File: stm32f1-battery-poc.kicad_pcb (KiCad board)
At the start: 4 copper layers, 92.5 x 85 mm, 153 parts, among them J1 Conn_01x02, J10 Conn_02x03_Odd_Even, J11 Conn_02x03_Odd_Even, J12 Conn_02x03_Odd_Even, J2 Conn_02x02_Odd_Even, J3 Conn_02x03_Odd_Even, J4 Conn_02x07_Odd_Even, J5 Conn_02x02_Odd_Even, J6 Conn_02x02_Odd_Even, J7 Conn_02x03_Odd_Even, J8 Conn_01x02, J9 Conn_01x04_Pin, M1 Stepper_Motor_bipolar, M2 Motor_3_Phases, Q1 Q_NMOS, Q2 Q_NMOS, SW1 SW_Push, SW2 SW_Push, SW3 SW_Push, SW4 SW_SPST, U1 LM78M05, U10 DRV8311H, U2 HT753-1, U3 SN65HVD230, U4 QRE1113GR, U5 QRE1113GR, U6 QRE1113GR, U7 DRV8424RGER, U8 STM32F103C8Tx, U9 BQ77905, Y1 8M

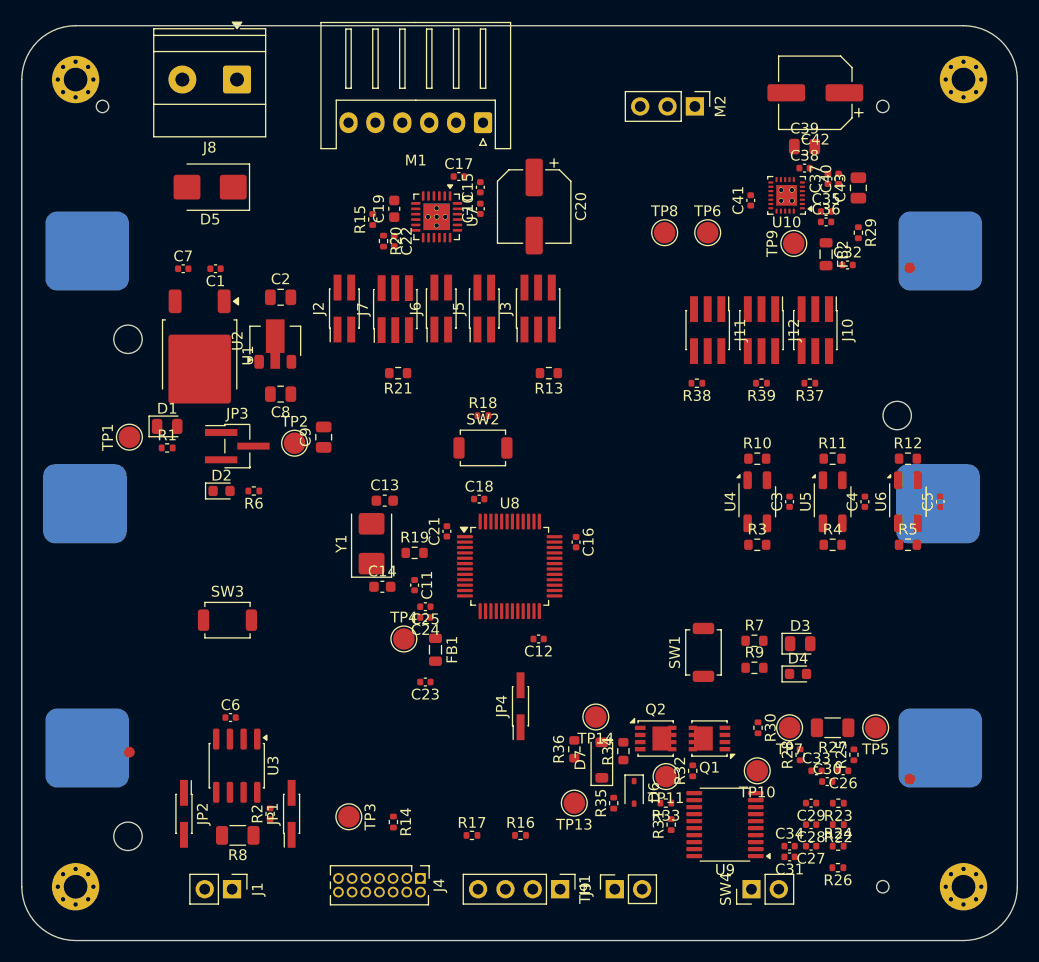
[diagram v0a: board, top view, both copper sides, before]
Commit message: pcb: add gnd planes
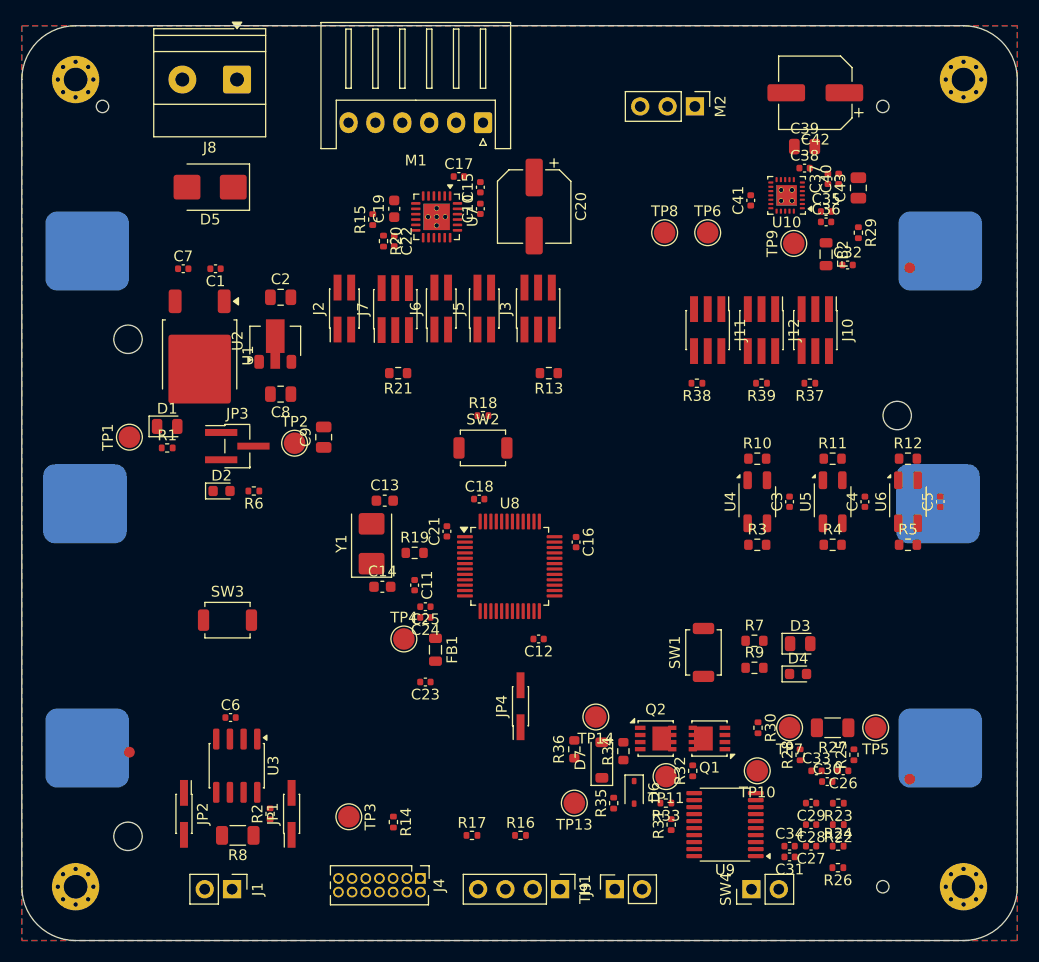
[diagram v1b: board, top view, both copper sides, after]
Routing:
- added copper zone on B.Cu, net GND
- added copper zone on F.Cu, net GND
- added copper zone on In1.Cu, net GND
- added copper zone on In2.Cu, net GND
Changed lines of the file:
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@@
 		(net 3)
+	)
+	(zone
+		(net 5)
+		(net_name "GND")
+		(layers "F.Cu" "B.Cu" "In1.Cu" "In2.Cu")
+		(hatch edge 0.5)
+		(connect_pads
+			(clearance 0.2)
+		)
+		(min_thickness 0.15)
+		(filled_areas_thickness no)
+		(fill yes
+			(thermal_gap 0.35)
+			(thermal_bridge_width 0.35)
+		)
+		(polygon
+			(pts
+				(xy 195 42.5) (xy 102.5 42.5) (xy 102.5 127.5) (xy 195 127.5)
+			)
+		)
 	)
 	(embedded_fonts no)

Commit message: pcb: add gnd vias
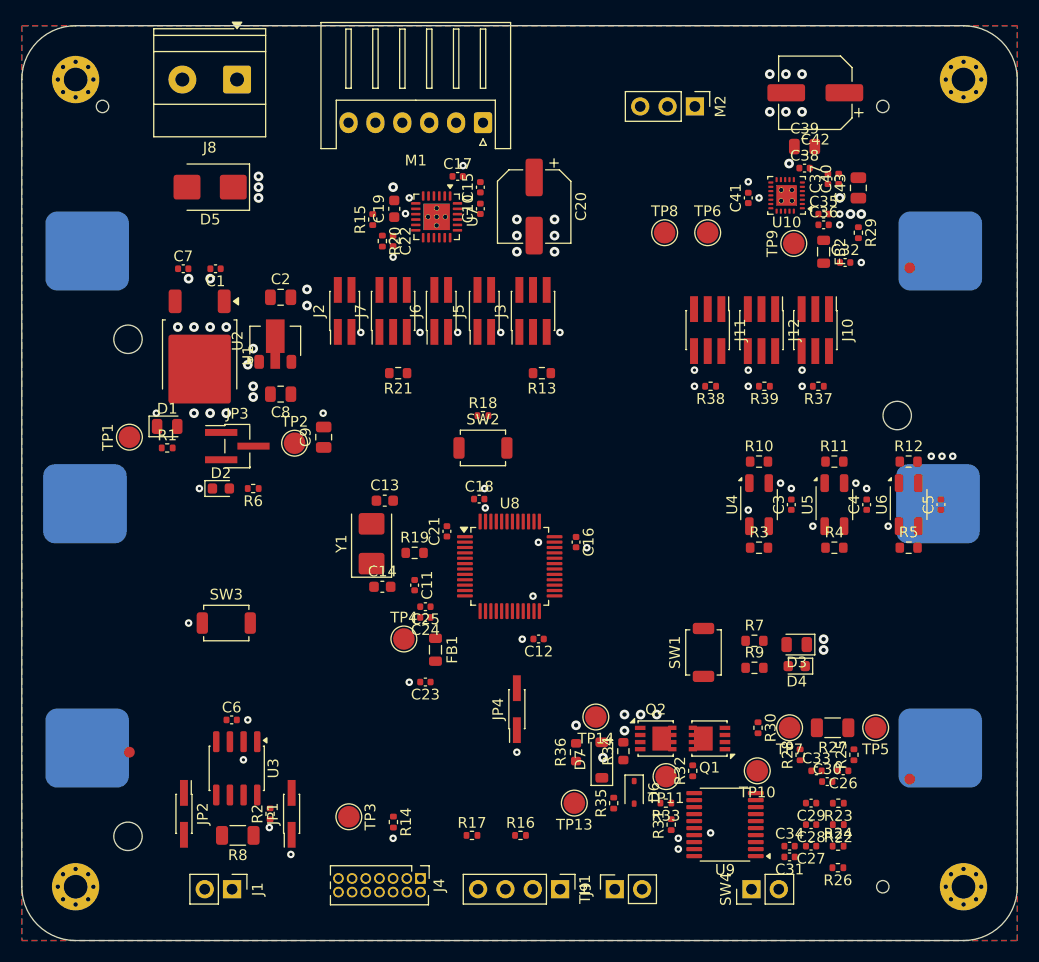
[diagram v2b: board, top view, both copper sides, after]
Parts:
- moved R38 1.30 mm to (166.5, 76.0)
- moved R37 0.84 mm to (176.5, 76.0)
- moved D4 0.74 mm to (174.5, 102.0), turned to 180 degrees
- moved R13 0.65 mm to (150.8, 74.8)
- moved J3 0.52 mm to (150.0, 69.0)
- moved JP4 0.43 mm to (148.5, 106.0)
- moved R39 0.39 mm to (171.5, 76.0)
- moved C36 0.35 mm to (177.0, 61.0)
- moved D3 0.34 mm to (174.5, 100.0), turned to 180 degrees
- moved C35 0.33 mm to (177.0, 60.0)
- moved C32 0.33 mm to (179.0, 64.5)
- moved C41 0.33 mm to (170.0, 58.5)
- moved FB2 0.33 mm to (177.0, 63.5)
- moved C3 0.32 mm to (174.0, 87.0)
- moved C4 0.32 mm to (181.0, 87.0)
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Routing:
- net GND: vias 0 -> 93

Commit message: schem: change I2C pins
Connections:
- J9 pad 2: /I2C1_SDA -> /I2C2_SDA
- J9 pad 4: /I2C1_SCL -> /I2C2_SCL
- R16 pad 1: /I2C1_SDA -> /I2C2_SDA
- R17 pad 1: /I2C1_SCL -> /I2C2_SCL
- U8 pad 21: unconnected-(U8-PB10-Pad21) -> /I2C2_SCL
- U8 pad 22: unconnected-(U8-PB11-Pad22) -> /I2C2_SDA
- U8 pad 45: /I2C1_SCL -> unconnected-(U8-PB8-Pad45)
- U8 pad 46: /I2C1_SDA -> unconnected-(U8-PB9-Pad46)

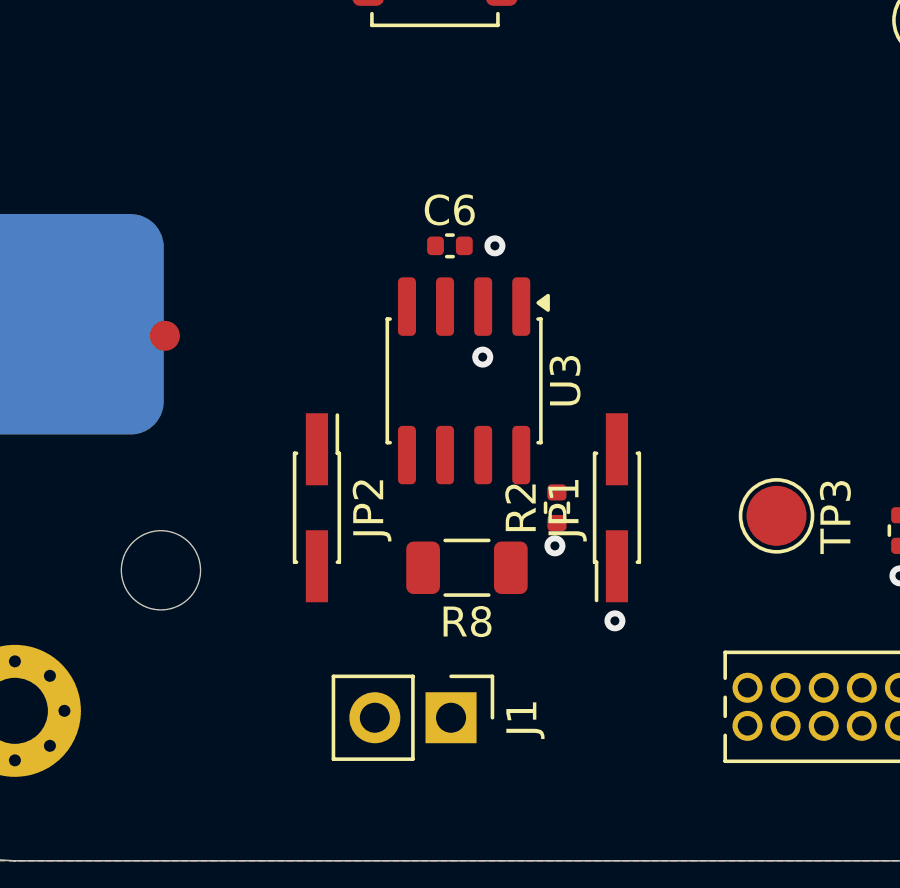
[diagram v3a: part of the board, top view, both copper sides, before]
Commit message: pcb: add CAN layout
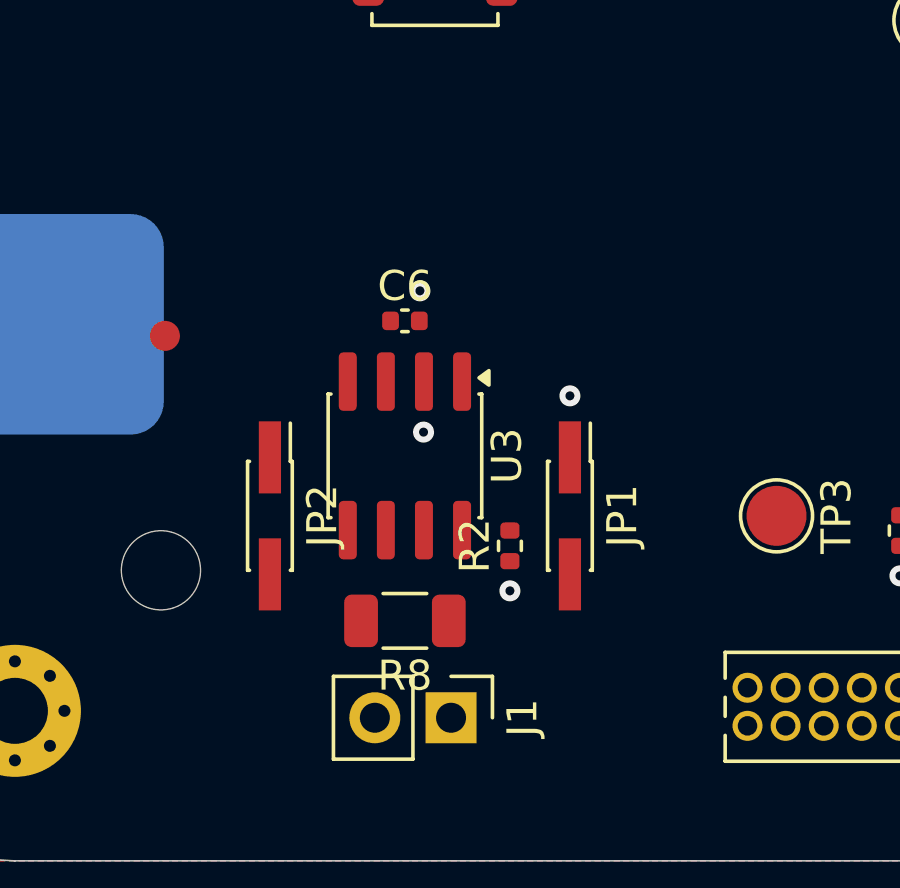
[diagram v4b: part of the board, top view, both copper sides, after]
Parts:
- moved U3 3.18 mm to (120.5, 114.0)
- moved C6 2.92 mm to (120.5, 109.5)
- moved R8 2.72 mm to (120.5, 119.5)
- moved R2 2.02 mm to (124.0, 117.0)
- moved JP1 1.59 mm to (126.0, 116.0), turned to -90 degrees
- moved JP2 1.59 mm to (116.0, 116.0)
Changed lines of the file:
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@@
 	(footprint "Connector_PinHeader_1.27mm:PinHeader_2x01_P1.27mm_Vertical_SMD"
 		(layer "F.Cu")
-		(at 117.5675 115.73 -90)
+		(at 116 116 -90)
 		(descr "surface-mounted straight pin header, 2x01, 1.27mm pitch, double rows")
 		(tags "Surface mounted pin header SMD 2x01 1.27mm double row")
@@
 	(footprint "Capacitor_SMD:C_0402_1005Metric"
 		(layer "F.Cu")
-		(at 122 107)
+		(at 120.5 109.5)
 		(descr "Capacitor SMD 0402 (1005 Metric), square (rectangular) end terminal, IPC-7351 nominal, (Body size source: IPC-SM-782 page 76, https://www.pcb-3d.com/wordpress/wp-content/uploads/ipc-sm-782a_amendment_1_and_2.pdf), generated with kicad-footprint-generator")
 		(tags "capacitor")
@@
 	(footprint "Resistor_SMD:R_0402_1005Metric"
 		(layer "F.Cu")
-		(at 125.5675 115.73 90)
+		(at 124 117 90)
 		(descr "Resistor SMD 0402 (1005 Metric), square (rectangular) end terminal, IPC-7351 nominal, (Body size source: IPC-SM-782 page 72, https://www.pcb-3d.com/wordpress/wp-content/uploads/ipc-sm-782a_amendment_1_and_2.pdf), generated with kicad-footprint-generator")
 		(tags "resistor")
@@
 	(footprint "Connector_PinHeader_1.27mm:PinHeader_2x01_P1.27mm_Vertical_SMD"
 		(layer "F.Cu")
-		(at 127.5675 115.73 90)
+		(at 126 116 -90)
 		(descr "surface-mounted straight pin header, 2x01, 1.27mm pitch, double rows")
 		(tags "Surface mounted pin header SMD 2x01 1.27mm double row")
@@
 		(attr smd exclude_from_bom)
 		(fp_line
-			(start 1.815 -0.745)
-			(end 1.815 -0.68)
+			(start -1.815 0.745)
+			(end 1.815 0.745)
 			(stroke
 				(width 0.12)
@@
 		)
 		(fp_line
-			(start -1.815 -0.745)
-			(end 1.815 -0.745)
+			(start -1.815 0.68)
+			(end -1.815 0.745)
 			(stroke
 				(width 0.12)
@@
 		)
 		(fp_line
-			(start -1.815 -0.745)
-			(end -1.815 -0.68)
+			(start 1.815 0.68)
+			(end 1.815 0.745)
 			(stroke
 				(width 0.12)
@@
 		)
 		(fp_line
-			(start 1.815 0.68)
-			(end 1.815 0.745)
+			(start -1.815 -0.745)
+			(end -1.815 -0.68)
 			(stroke
 				(width 0.12)
@@
 		)
 		(fp_line
-			(start -1.815 0.68)
-			(end -1.815 0.745)
+			(start -1.815 -0.745)
+			(end 1.815 -0.745)
 			(stroke
 				(width 0.12)
@@
 		)
 		(fp_line
-			(start -1.815 0.745)
-			(end 1.815 0.745)
+			(start 1.815 -0.745)
+			(end 1.815 -0.68)
 			(stroke
 				(width 0.12)
@@
 		)
 		(fp_line
-			(start 4.29 -1.14)
-			(end -4.29 -1.14)
+			(start -4.29 1.14)
+			(end 4.29 1.14)
 			(stroke
 				(width 0.05)
@@
 		)
 		(fp_line
-			(start -4.29 -1.14)
-			(end -4.29 1.14)
+			(start 4.29 1.14)
+			(end 4.29 -1.14)
 			(stroke
 				(width 0.05)
@@
 		)
 		(fp_line
-			(start 4.29 1.14)
-			(end 4.29 -1.14)
+			(start -4.29 -1.14)
+			(end -4.29 1.14)
 			(stroke
 				(width 0.05)
@@
 		)
 		(fp_line
-			(start -4.29 1.14)
-			(end 4.29 1.14)
+			(start 4.29 -1.14)
+			(end -4.29 -1.14)
 			(stroke
 				(width 0.05)
@@
 		)
 		(fp_line
-			(start 1.705 -0.635)
-			(end 1.705 0.635)
+			(start -1.705 0.635)
+			(end -1.705 -0.2)
 			(stroke
 				(width 0.1)
@@
 		)
 		(fp_line
-			(start -1.27 -0.635)
-			(end 1.705 -0.635)
+			(start 1.705 0.635)
+			(end -1.705 0.635)
 			(stroke
 				(width 0.1)
@@
 		)
 		(fp_line
-			(start 2.75 -0.2)
-			(end 2.75 0.2)
+			(start -2.75 0.2)
+			(end -1.705 0.2)
 			(stroke
 				(width 0.1)
@@
 		)
 		(fp_line
-			(start 1.705 -0.2)
-			(end 2.75 -0.2)
+			(start 2.75 0.2)
+			(end 1.705 0.2)
 			(stroke
 				(width 0.1)
@@
 		)
 		(fp_line
-			(start -1.705 -0.2)
-			(end -1.27 -0.635)
+			(start -2.75 -0.2)
+			(end -2.75 0.2)
 			(stroke
 				(width 0.1)
@@
 		)
 		(fp_line
-			(start -2.75 -0.2)
-			(end -2.75 0.2)
+			(start -1.705 -0.2)
+			(end -1.27 -0.635)
 			(stroke
 				(width 0.1)
@@
 		)
 		(fp_line
-			(start 2.75 0.2)
-			(end 1.705 0.2)
+			(start 1.705 -0.2)
+			(end 2.75 -0.2)
 			(stroke
 				(width 0.1)
@@
 		)
 		(fp_line
-			(start -2.75 0.2)
-			(end -1.705 0.2)
+			(start 2.75 -0.2)
+			(end 2.75 0.2)
 			(stroke
 				(width 0.1)
@@
 		)
 		(fp_line
-			(start 1.705 0.635)
-			(end -1.705 0.635)
+			(start -1.27 -0.635)
+			(end 1.705 -0.635)
 			(stroke
 				(width 0.1)
@@
 		)
 		(fp_line
-			(start -1.705 0.635)
-			(end -1.705 -0.2)
+			(start 1.705 -0.635)
+			(end 1.705 0.635)
 			(stroke
 				(width 0.1)
@@
 		)
 		(pad "1" smd rect
-			(at -1.95 0 90)
+			(at -1.95 0 270)
 			(size 2.4 0.74)
 			(layers "F.Cu" "F.Mask" "F.Paste")
@@
 		)
 		(pad "2" smd rect
-			(at 1.95 0 90)
+			(at 1.95 0 270)
 			(size 2.4 0.74)
 			(layers "F.Cu" "F.Mask" "F.Paste")
@@
 	(footprint "Package_SO:SOIC-8_3.9x4.9mm_P1.27mm"
 		(layer "F.Cu")
-		(at 122.4725 111.5 -90)
+		(at 120.5 114 -90)
 		(descr "SOIC, 8 Pin (JEDEC MS-012AA, https://www.analog.com/media/en/package-pcb-resources/package/pkg_pdf/soic_narrow-r/r_8.pdf), generated with kicad-footprint-generator ipc_gullwing_generator.py")
 		(tags "SOIC SO")
@@
 	(footprint "Resistor_SMD:R_1206_3216Metric"
 		(layer "F.Cu")
-		(at 122.5675 117.73 180)
+		(at 120.5 119.5 180)
 		(descr "Resistor SMD 1206 (3216 Metric), square (rectangular) end terminal, IPC-7351 nominal, (Body size source: IPC-SM-782 page 72, https://www.pcb-3d.com/wordpress/wp-content/uploads/ipc-sm-782a_amendment_1_and_2.pdf), generated with kicad-footprint-generator")
 		(tags "resistor")
@@
 	)
 	(via
-		(at 125.5 117)
+		(at 124 118.5)
 		(size 0.7)
 		(drill 0.3)
@@
 	)
 	(via
-		(at 123.093312 110.708542)
+		(at 121.120812 113.208542)
 		(size 0.7)
 		(drill 0.3)
@@
 	)
 	(via
-		(at 123.5 107)
+		(at 121 108.5)
 		(size 0.7)
 		(drill 0.3)
@@
 	)
 	(via
-		(at 127.5 119.5)
+		(at 126 112)
 		(size 0.7)
 		(drill 0.3)

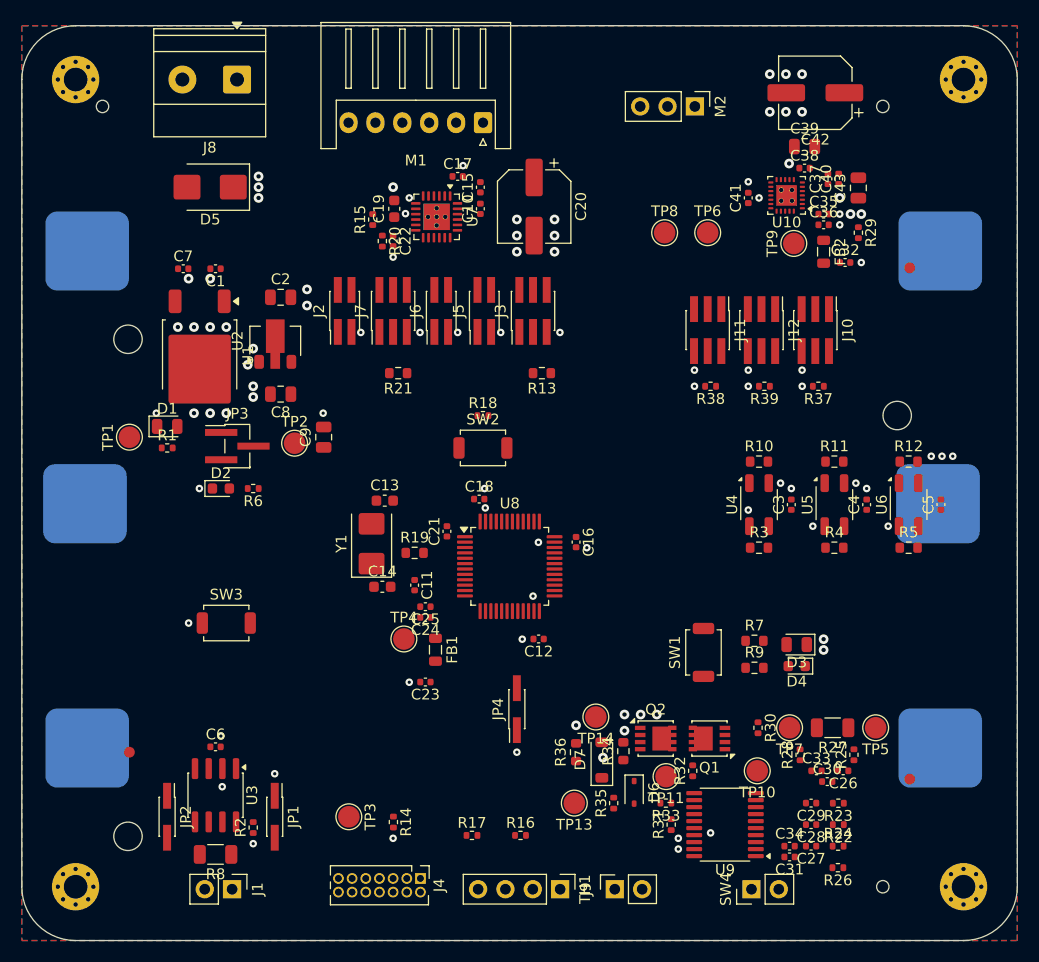
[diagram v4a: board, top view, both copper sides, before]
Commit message: pcb: add STDC14 debug port routing
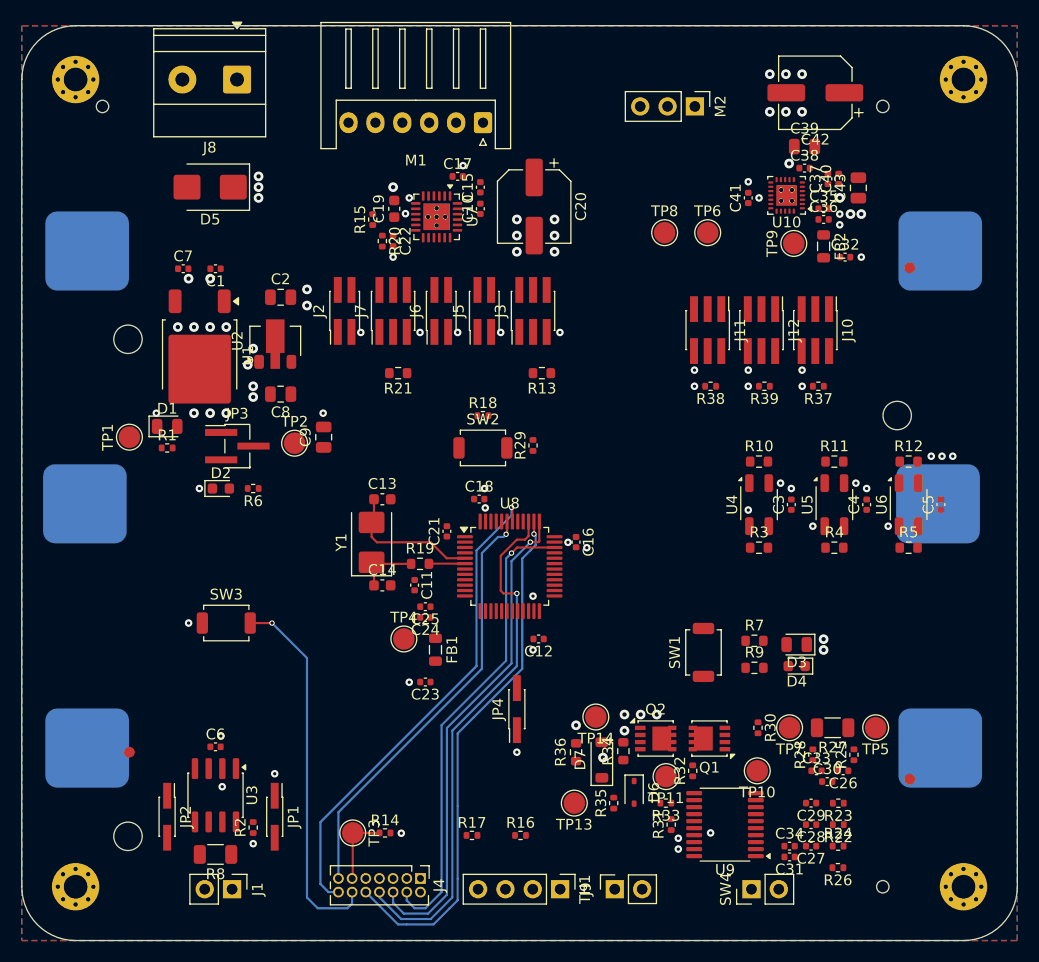
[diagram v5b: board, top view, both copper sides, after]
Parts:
- moved R29 36.1 mm to (150.0, 81.5), turned to 90 degrees
- moved TP3 1.54 mm to (133.2, 117.5)
- moved R14 1.27 mm to (136.2, 117.5), turned to 0 degrees
- moved R28 1.18 mm to (176.0, 110.2)
- moved R19 1.14 mm to (139.5, 92.5)
- moved C32 0.50 mm to (179.0, 64.0)
- moved C35 0.50 mm to (177.0, 59.5)
- moved C36 0.50 mm to (177.0, 60.5)
- moved FB2 0.50 mm to (177.0, 63.0)
- moved C13 0.26 mm to (136.0, 86.5)
- moved C14 0.13 mm to (136.0, 94.5)
- moved Y1 0.13 mm to (135.0, 90.5)
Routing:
- net /SYS_JTDO: track 0.00 -> 49.2 mm, vias 0 -> 1
- net /SYS_JTDI: track 0.00 -> 49.0 mm, vias 0 -> 1
- net /SYS_JTCK: track 0.00 -> 45.8 mm, vias 0 -> 1
- net /USART1_TX: track 0.00 -> 45.7 mm, vias 0 -> 1
- net /SYS_JTMS: track 0.00 -> 43.3 mm, vias 0 -> 1
- net /USART1_RX: track 0.00 -> 39.9 mm, vias 0 -> 1
- net /NRST: track 0.00 -> 34.7 mm, vias 0 -> 1
- net /XTAL_I: track 0.00 -> 13.1 mm
- net Net-(J4-Pin_11): track 0.00 -> 6.74 mm
- net /XTAL_RO: track 0.00 -> 5.98 mm
- net /XTAL_O: track 0.00 -> 3.36 mm
